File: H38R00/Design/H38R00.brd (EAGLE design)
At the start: 34.6 x 60 mm, 1 part, among them P1 HEXABIT_17.32_X2_POWER_ONLY

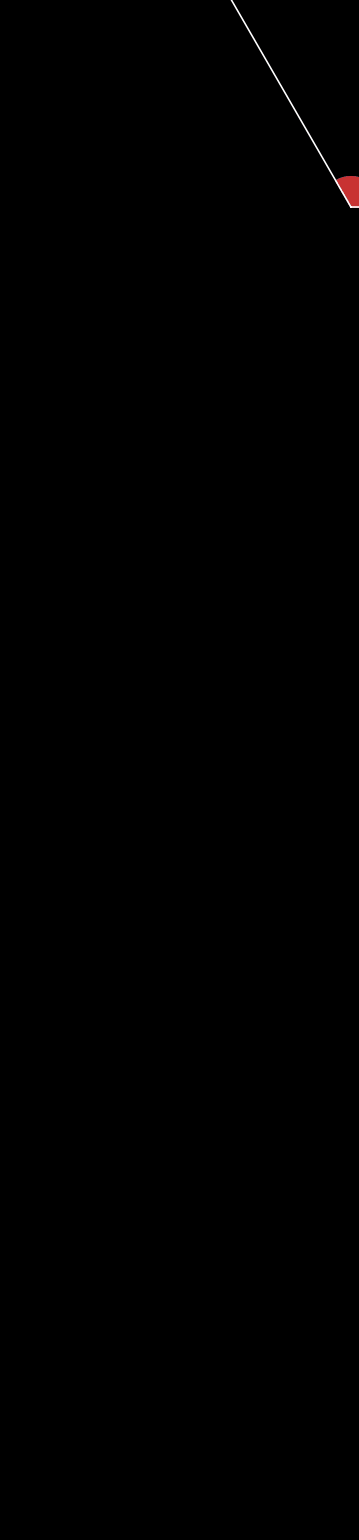
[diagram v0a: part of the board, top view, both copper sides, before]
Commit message: Added main ICs and some passives
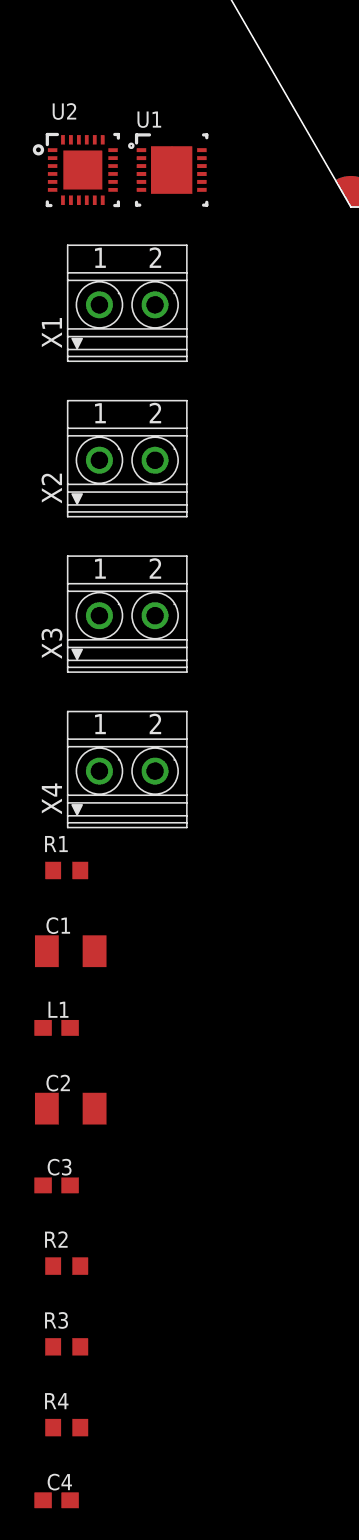
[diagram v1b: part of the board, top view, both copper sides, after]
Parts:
- added C1, C2: 2.2uF, Hexabitz:C1206K
- added C3: 100nF, Hexabitz:C-0603
- added C4: 1nF, Hexabitz:C-0603
- added L1: 2.2uH, Hexabitz:C-0603
- added R1: 1.00, Hexabitz:R-0603
- added R2: 113K, Hexabitz:R-0603
- added R3: 16.9K, Hexabitz:R-0603
- added R4: 2.00k, Hexabitz:R-0603
- added U1: LM5160DNT, Hexabitz:DNT0012B
- added U2: TPS65130RGERT, Hexabitz:RGE0024B_NV
- added X1: INPUT, Hexabitz:CON-PHOENIX-350_1751248
- added X2: OUT-15P, Hexabitz:CON-PHOENIX-350_1751248
- added X3: OUT-15N, Hexabitz:CON-PHOENIX-350_1751248
- added X4: OUT-5P, Hexabitz:CON-PHOENIX-350_1751248
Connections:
- removed net VDD: P1.PAD_PU11, P1.PAD_PU12, P1.PAD_PU13, P1.PAD_PU14, P1.PAD_PU15, P1.PAD_PU16, P1.PAD_PU17, P1.PAD_PU18, P1.PAD_PU19, P1.PAD_PU20
- new net AGND: U2.19
- new net BST: U1.10
- new net GND1: P1.PAD_PD11
- new net GND10: P1.PAD_PD20
- new net GND2: P1.PAD_PD12
- new net GND3: P1.PAD_PD13
- new net GND4: P1.PAD_PD14
- new net GND5: P1.PAD_PD15
- new net GND6: P1.PAD_PD16
- new net GND7: P1.PAD_PD17
- new net GND8: P1.PAD_PD18
- new net GND9: P1.PAD_PD19
- new net INN: U2.6
- new net INN_2: U2.5
- new net INP: U2.24
- new net INP_2: U2.1
- new net N$1: R1.1, X1.2
- new net N$2: C1.1, L1.1, R1.2
- new net N$3: C2.1, C3.1, L1.2, R2.1, R3.2, U1.3
- new net N$4: R2.2, U1.5
- new net N$5: R3.1, R4.2, U1.4
- new net N$6: C4.1, U1.6
- new net OUTN: U2.14
- new net OUTN_2: U2.13
- new net PAD: U2.25
- new net PGND: U2.3
- new net PGND_2: U2.2
- new net SW: U1.12
- new net SW_2: U1.11
- new net VCC: U1.9
- new net VDD1: P1.PAD_PU11
- new net VDD10: P1.PAD_PU20
- new net VDD2: P1.PAD_PU12
- new net VDD3: P1.PAD_PU13
- new net VDD4: P1.PAD_PU14
- new net VDD5: P1.PAD_PU15
- new net VDD6: P1.PAD_PU16
- new net VDD7: P1.PAD_PU17
- new net VDD8: P1.PAD_PU18
- new net VDD9: P1.PAD_PU19
- new net VIN: U2.4
- net GND: now also C1.2, C2.2, C3.2, C4.2, R4.1, U1.1, U1.13, U1.2, X1.1; no longer P1.PAD_PD11, P1.PAD_PD12, P1.PAD_PD13, P1.PAD_PD14, P1.PAD_PD15, P1.PAD_PD16, P1.PAD_PD17, P1.PAD_PD18, P1.PAD_PD19, P1.PAD_PD20

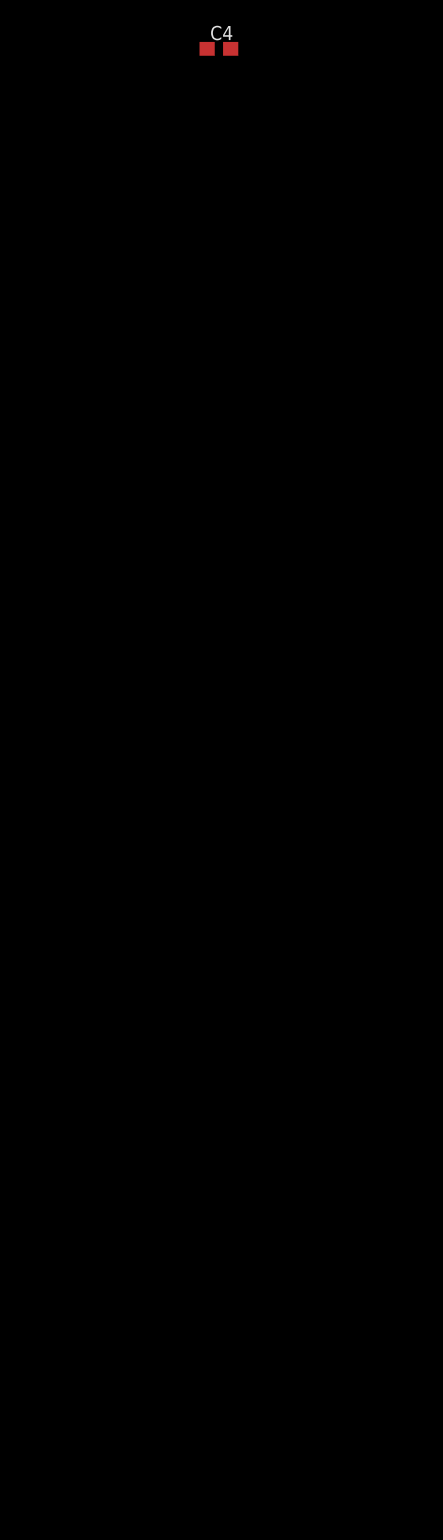
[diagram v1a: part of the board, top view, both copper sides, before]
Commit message: Finished the buck part
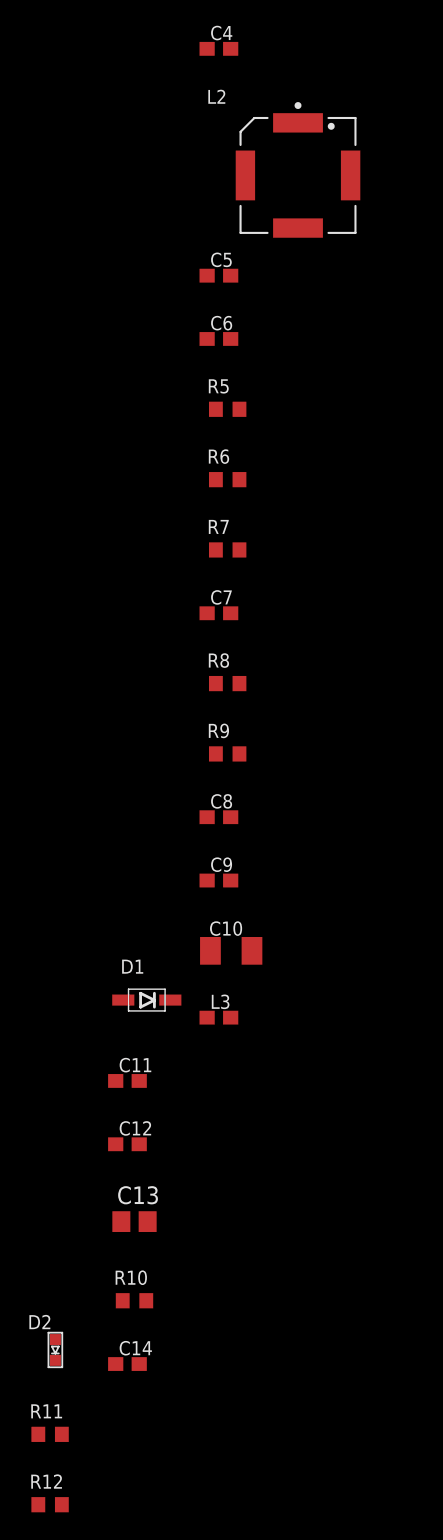
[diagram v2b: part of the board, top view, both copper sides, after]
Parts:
- added C10: 2.2uF, Hexabitz:C1206K
- added C11: 220nF, Hexabitz:C-0603
- added C12, C7: 100nF, Hexabitz:C-0603
- added C13: 10uF, Hexabitz:C-0805
- added C14: 100pF, Hexabitz:C-0603
- added C5: 10nF, Hexabitz:C-0603
- added C6: 1uF, Hexabitz:C-0603
- added C8, C9: 22nF, Hexabitz:C-0603
- added D1: DIOD-SOD-123, Hexabitz:SOD123
- added D2: GREEN, Hexabitz:VLMS1300-GS08
- added L2: 22uH, Hexabitz:WUERTH_ELEKTRONIK_74489430220_0
- added L3: 2.2uH, Hexabitz:C-0603
- added R10: 150, Hexabitz:R-0603
- added R11: 1.21K, Hexabitz:R-0603
- added R12, R8: 0.0, Hexabitz:R-0603
- added R5: 27.4K, Hexabitz:R-0603
- added R6: 3.48K, Hexabitz:R-0603
- added R7: 2.00K, Hexabitz:R-0603
- added R9: 42.4, Hexabitz:R-0603
- R4: value 2.00k -> 2.00K
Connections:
- removed net BST: U1.10
- removed net SW: U1.12
- removed net SW_2: U1.11
- removed net VCC: U1.9
- new net N$10: C7.2, R6.1, R7.2, R9.2, U1.8
- new net N$11: C7.1, R5.2
- new net N$12: C9.1, R6.2, R8.1
- new net N$13: L2.2, R8.2
- new net N$14: C8.1, R9.1
- new net N$15: C11.1, C14.2, D1.2, L3.1
- new net N$16: D1.1, L2.4, R10.2
- new net N$17: C14.1, R10.1
- new net N$18: C12.1, C13.1, L3.2, R12.1, X4.1
- new net N$19: R11.2, R12.2
- new net N$20: D2.A, R11.1
- new net N$7: C5.2, L2.3, R5.1, U1.11, U1.12
- new net N$8: C5.1, U1.10
- new net N$9: C6.1, U1.7, U1.9
- net AGND: now also C10.2, C11.2, C12.2, C13.2, D2.C, L2.1, X4.2
- net GND: now also C10.1, C6.2, C8.2, C9.2, R7.1

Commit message: Finished schematics
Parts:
- added C15, C24, C25, C26, C27: 10uF, Hexabitz:C-0805
- added C16, C17, C20, C21: 100nF, Hexabitz:C-0603
- added C18: 4700pF, Hexabitz:C-0603
- added C19: 10nF, Hexabitz:C-0603
- added C22, C23: 1uF, Hexabitz:C-0603
- added C28: 5.6pF, Hexabitz:C-0603
- added C29: 220nF, Hexabitz:C-0603
- added C30: 6.8pF, Hexabitz:C-0603
- added D3, D4: DIOD-SOD-123, Hexabitz:SOD123
- added D5, D6: GREEN, Hexabitz:VLMS1300-GS08
- added FB1: 600 Ohm, Hexabitz:FB-0603
- added L4, L5: 10uH, Hexabitz:WUERTH_ELEKTRONIK_74404024100_0
- added R13: 100.0, Hexabitz:R-0603
- added R14, R15: 1.00, Hexabitz:R-0603
- added R16: 1.30M, Hexabitz:R-0603
- added R17: 86.6K, Hexabitz:R-0603
- added R18: 976K, Hexabitz:R-0603
- added R19, R20: 5.36K, Hexabitz:R-0603
- added SJ1, SJ2, SJ3: (no value), jumper:SJ
- R12: value 0.0 -> 105K
- moved R12 119.9 mm to (-52.7, -286.0)
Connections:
- removed net INN: U2.6
- removed net INN_2: U2.5
- removed net INP: U2.24
- removed net INP_2: U2.1
- removed net OUTN: U2.14
- removed net OUTN_2: U2.13
- removed net PAD: U2.25
- removed net PGND: U2.3
- removed net PGND_2: U2.2
- removed net VIN: U2.4
- new net +15V: C24.1, C25.1, R14.2, SJ2.1, X2.1
- new net +5V: C12.1, C13.1, FB1.1, L3.2, SJ1.1, X4.1
- new net -15V: C26.2, C27.2, R15.2, SJ3.2, X3.2
- new net N$21: D3.1, L4.2, U2.1, U2.24
- new net N$22: C21.1, C23.1, C30.2, D3.2, R14.1, R18.1, U2.23
- new net N$23: C17.1, R13.1, U2.10, U2.11, U2.4, U2.8, U2.9
- new net N$24: C18.1, U2.18
- new net N$25: C19.1, U2.21
- new net N$26: D4.2, L5.1, U2.13, U2.14
- new net N$27: C20.2, C22.2, C28.2, D4.1, R15.1, R16.1, U2.15
- new net N$28: C28.1, R12.1, R16.2, U2.16
- new net N$29: C29.1, R12.2, U2.17
- new net N$30: C30.1, R17.2, R18.2, U2.22
- new net N$31: R19.1, SJ2.2
- new net N$32: D5.A, R19.2
- new net N$33: R20.1, SJ3.1
- new net N$34: D6.C, R20.2
- net AGND: now also C15.2, C16.2, C17.2, C18.2, C19.2, C20.1, C21.2, C22.1, C23.2, C24.2, C25.2, C26.1, C27.1, C29.2, D5.C, D6.A, L5.2, R17.1, U2.2, U2.25, U2.3, X2.2, X3.1
- net N$18: now also C15.1, C16.1, FB1.2, L4.1, R13.2, U2.5, U2.6; no longer C12.1, C13.1, L3.2, R12.1, X4.1
- net N$19: now also SJ1.2; no longer R12.2

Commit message: Renumber components Update transformer package Place connectors and half components
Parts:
- removed X1: INPUT, Hexabitz:CON-PHOENIX-350_1751248
- removed X2: OUT-15P, Hexabitz:CON-PHOENIX-350_1751248
- removed X3: OUT-15N, Hexabitz:CON-PHOENIX-350_1751248
- removed X4: OUT-5P, Hexabitz:CON-PHOENIX-350_1751248
- added +15V: OUT-15P, Hexabitz:CON-PHOENIX-350_1751248
- added +5V: OUT-5P, Hexabitz:CON-PHOENIX-350_1751248
- added -15V: OUT-15N, Hexabitz:CON-PHOENIX-350_1751248
- added IN: INPUT, Hexabitz:CON-PHOENIX-350_1751248
- C10: value 2.2uF -> 4700pF; device Hexabitz:C1206K -> Hexabitz:C-0603
- C11: value 220nF -> 100nF
- C12: value 100nF -> 5.6pF
- C13: value 10uF -> 6.8pF; device Hexabitz:C-0805 -> Hexabitz:C-0603
- C14: value 100pF -> 22nF
- C15: value 10uF -> 10nF; device Hexabitz:C-0805 -> Hexabitz:C-0603
- C16: value 100nF -> 220nF
- C17: value 100nF -> 2.2uF
- C18: value 4700pF -> 100nF
- C19, C5: value 10nF -> 100nF
- C20: value 100nF -> 1nF; device Hexabitz:C-0603 -> Hexabitz:C1206K
- C21: value 100nF -> 1uF
- C23: value 1uF -> 100pF
- C24: value 10uF -> 220nF; device Hexabitz:C-0805 -> Hexabitz:C-0603
- C28: value 5.6pF -> 10uF; device Hexabitz:C-0603 -> Hexabitz:C-0805
- C29: value 220nF -> 10uF; device Hexabitz:C-0603 -> Hexabitz:C-0805
- C3: value 100nF -> 10uF; device Hexabitz:C-0603 -> Hexabitz:C-0805
- C30: value 6.8pF -> 100nF
- C4: value 1nF -> 100nF
- C6: value 1uF -> 100nF
- C7: value 100nF -> 1nF
- C8: value 22nF -> 10nF
- C9: value 22nF -> 1uF
- D2: value GREEN -> DIOD-SOD-123; device Hexabitz:VLMS1300-GS08 -> Hexabitz:SOD123
- D4: value DIOD-SOD-123 -> GREEN; device Hexabitz:SOD123 -> Hexabitz:VLMS1300-GS08
- L2: value 22uH -> 10uH; device Hexabitz:WUERTH_ELEKTRONIK_74489430220_0 -> Hexabitz:WUERTH_ELEKTRONIK_74404024100_0
- L3: value 2.2uH -> 10uH; device Hexabitz:C-0603 -> Hexabitz:WUERTH_ELEKTRONIK_74404024100_0
- L4: value 10uH -> 22uH; device Hexabitz:WUERTH_ELEKTRONIK_74404024100_0 -> Hexabitz:WUERTH_ELEKTRONIK_74489430220_0
- L5: value 10uH -> 2.2uH; device Hexabitz:WUERTH_ELEKTRONIK_74404024100_0 -> Hexabitz:C-0603
- R10: value 150 -> 1.30M
- R11: value 1.21K -> 86.6K
- R12: value 105K -> 3.48K
- R13: value 100.0 -> 42.4
- R14: value 1.00 -> 0.0
- R15: value 1.00 -> 150
- R16: value 1.30M -> 1.00
- R17: value 86.6K -> 1.00
- R18: value 976K -> 5.36K
- R2: value 113K -> 16.9K
- R20: value 5.36K -> 1.21K
- R3: value 16.9K -> 2.00K
- R4: value 2.00K -> 100.0
- R5: value 27.4K -> 113K
- R6: value 3.48K -> 105K
- R7: value 2.00K -> 976K
- R8: value 0.0 -> 27.4K
- R9: value 42.4 -> 2.00K
- moved C27 489.6 mm to (37.6, 200.9)
- moved C28 486.5 mm to (37.6, 182.2)
- moved C25 471.3 mm to (37.6, 194.7)
- moved C26 471.3 mm to (37.6, 188.5)
- moved D6 471.3 mm to (25.8, 130.0)
- moved R19 471.3 mm to (37.6, 138.3)
- moved C21 462.3 mm to (37.1, 206.5)
- moved SJ2 461.0 mm to (31.6, 132.8)
- moved R18 447.4 mm to (31.5, 129.0)
- moved C18 437.6 mm to (37.1, 215.6)
- moved R20 416.6 mm to (28.2, 73.9), flipped to the bottom, turned to 270 degrees
- moved R17 416.2 mm to (51.6, 102.2)
- moved D5 409.9 mm to (28.2, 77.5), turned to 180 degrees
- moved SJ3 409.9 mm to (29.0, 70.7), flipped to the bottom
- moved R16 402.0 mm to (51.6, 97.2)
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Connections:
- net +15V: now also +15V.1, C27.1, R16.2, SJ1.1; no longer C24.1, R14.2, SJ2.1, X2.1
- net +5V: now also +5V.1, C29.1, C30.1, L5.2, SJ3.1; no longer C12.1, C13.1, L3.2, SJ1.1, X4.1
- net -15V: now also -15V.2, C28.2, R17.2, SJ2.2; no longer C27.2, R15.2, SJ3.2, X3.2
- net AGND: now also +15V.2, +5V.2, -15V.1, C19.1, C20.2, C27.2, C28.1, C3.2, C30.2, C5.2, C6.2, D4.C, L3.2, L4.1, R11.1; no longer C11.2, C12.2, C13.2, C17.2, C19.2, C20.1, C23.2, C27.1, D2.C, L2.1, L5.2, R17.1, X2.2, X3.1, X4.2
- net GND: now also C14.2, C17.2, C20.1, C7.2, IN.1, R3.1, R9.1; no longer C10.1, C3.2, C6.2, C8.2, R4.1, R7.1, X1.1
- net N$1: now also IN.2; no longer X1.2
- net N$10: now also C11.2, R12.1, R13.2; no longer C7.2, R6.1, R7.2
- net N$11: now also C11.1, R8.2; no longer C7.1, R5.2
- net N$12: now also C17.1, R12.2, R14.1; no longer C9.1, R6.2, R8.1
- net N$13: now also L4.2, R14.2; no longer L2.2, R8.2
- net N$14: now also C14.1, R13.1; no longer C8.1, R9.1
- net N$15: now also C23.2, C24.1, D3.2, L5.1; no longer C11.1, C14.2, D1.2, L3.1
- net N$16: now also D3.1, L4.4, R15.2; no longer D1.1, L2.4, R10.2
- net N$17: now also C23.1, R15.1; no longer C14.1, R10.1
- net N$18: now also C3.1, C5.1, L2.1, R4.2; no longer C15.1, C16.1, L4.1, R13.2
- net N$19: now also R20.2, SJ3.2; no longer R11.2, SJ1.2
- net N$20: now also D5.A, R20.1; no longer D2.A, R11.1
- net N$21: now also D1.1, L2.2; no longer D3.1, L4.2
- net N$22: now also C13.2, C18.1, D1.2, R16.1, R7.1; no longer C23.1, C30.2, D3.2, R14.1, R18.1
- net N$23: now also C6.1, R4.1; no longer C17.1, R13.1
- net N$24: now also C10.1; no longer C18.1
- net N$25: now also C15.1; no longer C19.1
- net N$26: now also D2.2, L3.1; no longer D4.2, L5.1
- net N$27: now also C12.2, C19.2, D2.1, R10.1, R17.1; no longer C20.2, C28.2, D4.1, R15.1, R16.1
- net N$28: now also C12.1, R10.2, R6.1; no longer C28.1, R12.1, R16.2
- net N$29: now also C16.1, R6.2; no longer C29.1, R12.2
- net N$3: now also C4.1, R2.2, R5.1; no longer C3.1, R2.1, R3.2
- net N$30: now also C13.1, R11.2, R7.2; no longer C30.1, R17.2, R18.2
- net N$31: now also SJ1.2; no longer SJ2.2
- net N$32: now also D4.A; no longer D5.A
- net N$33: now also R18.1, SJ2.1; no longer R20.1, SJ3.1
- net N$34: now also R18.2; no longer R20.2
- net N$4: now also R5.2; no longer R2.2
- net N$5: now also R2.1, R3.2; no longer R3.1, R4.2
- net N$6: now also C7.1; no longer C4.1
- net N$7: now also C8.2, L4.3, R8.1; no longer C5.2, L2.3, R5.1
- net N$8: now also C8.1; no longer C5.1
- net N$9: now also C9.1; no longer C6.1

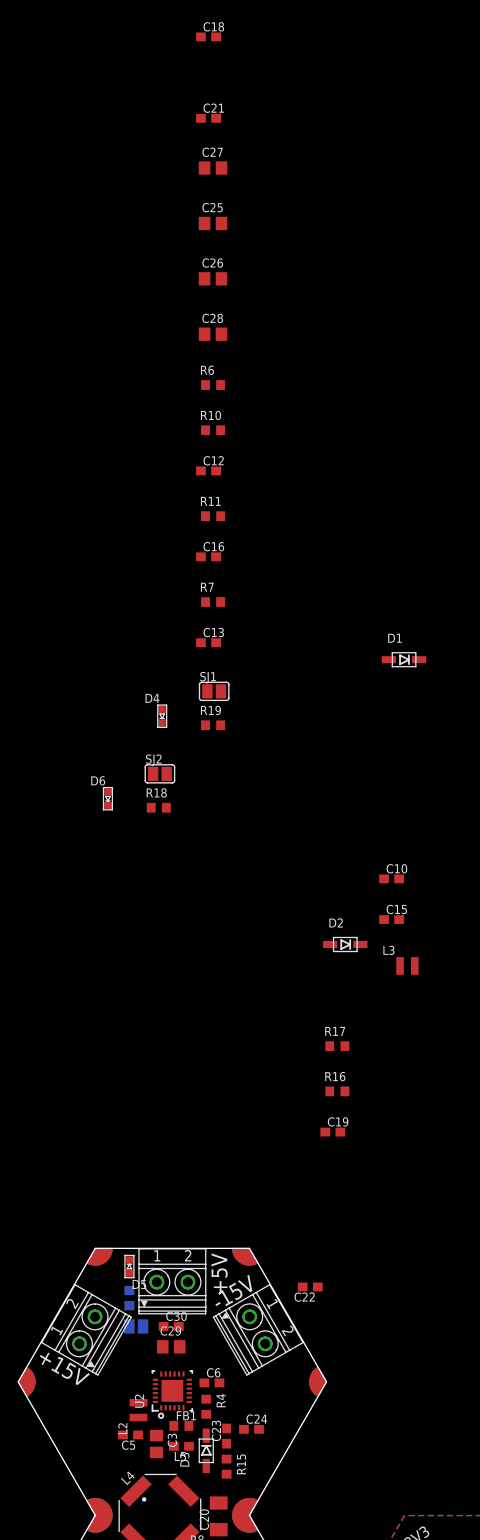
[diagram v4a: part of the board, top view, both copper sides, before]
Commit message: All components placed inside board!
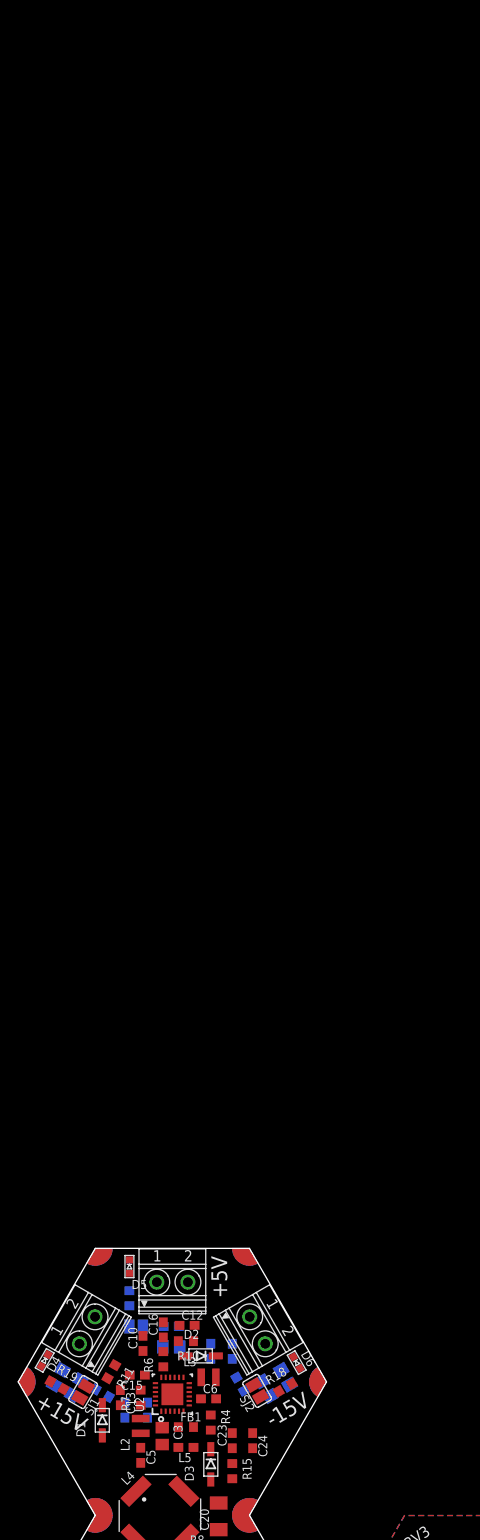
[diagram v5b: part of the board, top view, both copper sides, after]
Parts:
- moved C18 154.5 mm to (30.2, 61.3), flipped to the bottom, turned to 270 degrees
- moved C21 145.5 mm to (27.7, 61.3), flipped to the bottom, turned to 270 degrees
- moved C27 137.9 mm to (22.2, 63.9), flipped to the bottom, turned to 300 degrees
- moved C25 130.8 mm to (20.2, 65.0), flipped to the bottom, turned to 300 degrees
- moved C26 124.9 mm to (43.6, 63.8), flipped to the bottom, turned to 60 degrees
- moved C28 117.5 mm to (45.7, 65.0), flipped to the bottom, turned to 60 degrees
- moved R6 109.6 mm to (32.0, 67.1), turned to 90 degrees
- moved R10 102.4 mm to (34.5, 69.1), turned to 180 degrees
- moved R11 96.8 mm to (26.2, 65.7), turned to 240 degrees
- moved C12 96.0 mm to (34.7, 70.9)
- moved D1 92.0 mm to (25.1, 60.2), turned to 90 degrees
- moved R7 89.8 mm to (29.5, 62.7), turned to 90 degrees
- moved C16 87.0 mm to (32.0, 70.4), turned to 90 degrees
- moved C13 85.4 mm to (27.2, 62.7), turned to 270 degrees
- moved SJ1 80.1 mm to (23.0, 63.4), turned to 240 degrees
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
